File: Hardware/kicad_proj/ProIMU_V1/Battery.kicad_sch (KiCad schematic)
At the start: 7 parts, among them U7 SPX2920M3-3.3_SOT223

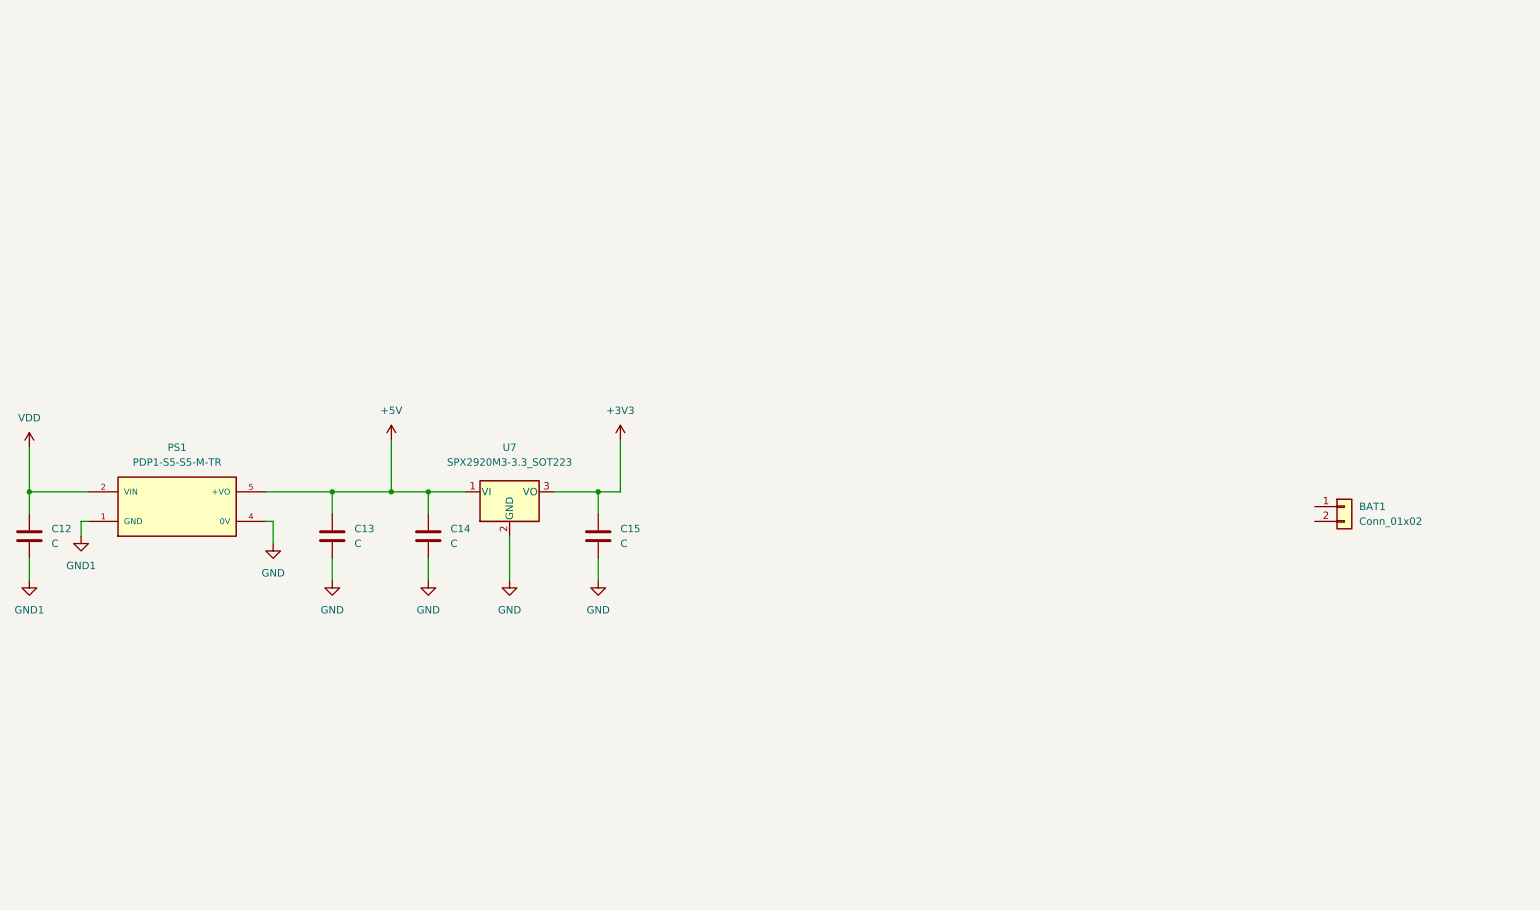
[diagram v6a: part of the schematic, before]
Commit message: Removed isolated DC-DC converter and added new regulator in place of it
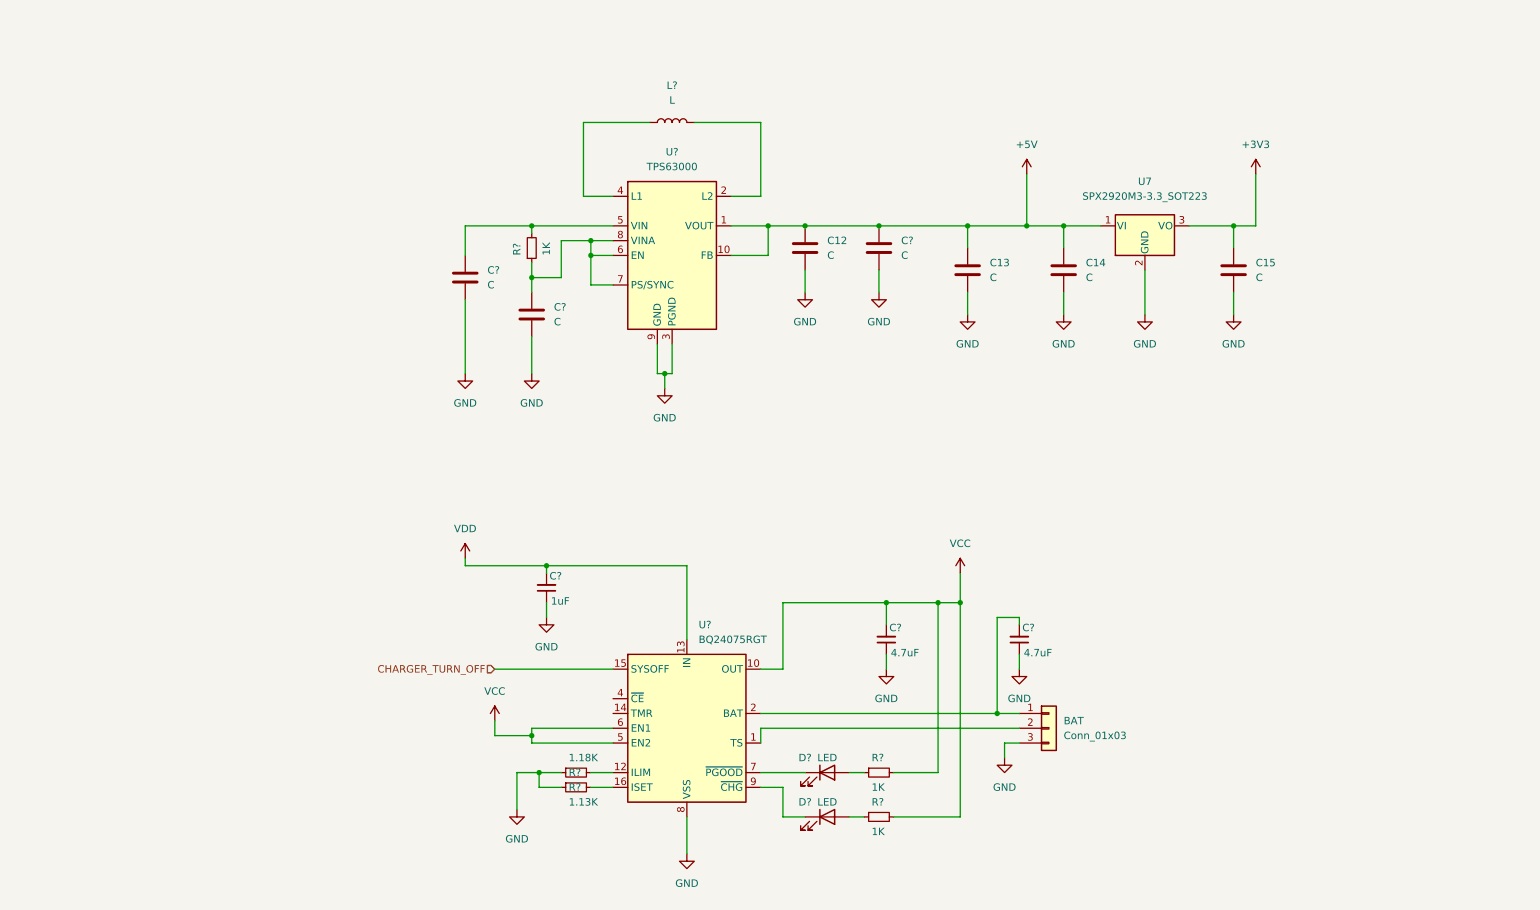
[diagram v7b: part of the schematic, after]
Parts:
- removed BAT1: Conn_01x02, Connector_PinHeader_2.54mm:PinHeader_1x02_P2.54mm_Vertical, symbol Connector_Generic:Conn_01x02
- removed PS1: PDP1-S5-S5-M-TR, footprints:CONV_PDP1-S5-S5-M-TR, symbol PDP1-S5-S5-M-TR:PDP1-S5-S5-M-TR
- added BAT: Conn_01x03, symbol Connector_Generic:Conn_01x03
- added C? (x3): C, Capacitor_SMD:C_0805_2012Metric_Pad1.18x1.45mm_HandSolder, symbol Device:C
- added C? (x2): 4.7uF, Capacitor_SMD:C_0402_1005Metric_Pad0.74x0.62mm_HandSolder, symbol Device:C_Small
- added C?: 1uF, Capacitor_SMD:C_0402_1005Metric_Pad0.74x0.62mm_HandSolder, symbol Device:C_Small
- added D? (x2): LED, symbol Device:LED
- added L?: L, symbol Device:L
- added R? (x3): 1K, Resistor_SMD:R_0402_1005Metric_Pad0.72x0.64mm_HandSolder, symbol Device:R_Small
- added R?: 1.18K, Resistor_SMD:R_0402_1005Metric_Pad0.72x0.64mm_HandSolder, symbol Device:R_Small
- added R?: 1.13K, Resistor_SMD:R_0402_1005Metric_Pad0.72x0.64mm_HandSolder, symbol Device:R_Small
- added U?: TPS63000, Package_SON:Texas_DRC0010J_ThermalVias, symbol Regulator_Switching:TPS63000
- added U?: BQ24075RGT, Package_DFN_QFN:VQFN-16-1EP_3x3mm_P0.5mm_EP1.6x1.6mm, symbol Battery_Management:BQ24075RGT
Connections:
- net GND1 is gone; now on net GND: C12.2
- net +5V: now also C12.1, C?.1, U?.1 (VOUT), U?.10 (FB)
- net GND: now also BAT.3 (Pin_3), C?.1, C?.1, C?.1, C?.2, C?.2, C?.2, R?.1, R?.1, U?.11 (PGND), U?.17 (VSS), U?.3 (PGND), U?.8 (VSS), U?.9 (GND)
- net VDD: now also C?.2, U?.13 (IN); no longer C12.1
- new net: L?.1, U?.4 (L1)
- new net: L?.2, U?.2 (L2)
- new net: BAT.1 (Pin_1), C?.2, U?.2 (BAT), U?.3 (BAT)
- new net: BAT.2 (Pin_2), U?.1 (TS)
- new net: C?.1, R?.2, U?.5 (VIN)
- new net: C?.1, R?.1, U?.6 (EN), U?.7 (PS/SYNC), U?.8 (VINA)
- new net: R?.2, U?.12 (ILIM)
- new net: R?.2, U?.16 (ISET)
- new net: D?.1 (K), U?.7 (~{PGOOD})
- new net: D?.1 (K), U?.9 (~{CHG})
- new net: D?.2 (A), R?.1 (x2)
- new net CHARGER_TURN_OFF: U?.15 (SYSOFF)
- new net VCC: C?.2, R?.2, R?.2, U?.10 (OUT), U?.11 (OUT), U?.5 (EN2), U?.6 (EN1)
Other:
- moved on the sheet: C12, C13, C14, C15, U7
